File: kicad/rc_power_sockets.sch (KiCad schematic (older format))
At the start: 24 parts, among them IC1 ATTINY85, J1 PIR, J2 433MHZ, J3 433MHZ, P1 ICSP, P2 CONN_GND, Q1 NMOS, Q2 PMOS, SW1 SPST, U1 MCP1700T

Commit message: Schematic update
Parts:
- MOUNT1, MOUNT2, MOUNT3, MOUNT4: footprint (none) -> Wire_Pads:SolderWirePad_single_2-5mmDrill
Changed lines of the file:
@@
 F 0 "MOUNT3" V 1800 1100 50  0000 C CNN
 F 1 "CONN_01X01" V 1600 800 50  0001 C CNN
-F 2 "" H 1700 1100 50  0000 C CNN
+F 2 "Wire_Pads:SolderWirePad_single_2-5mmDrill" H 1700 1100 50  0001 C CNN
 F 3 "" H 1700 1100 50  0000 C CNN
 	1    1700 1100
@@
 F 0 "MOUNT4" V 2250 1100 50  0000 C CNN
 F 1 "CONN_01X01" V 2050 800 50  0001 C CNN
-F 2 "" H 2150 1100 50  0000 C CNN
+F 2 "Wire_Pads:SolderWirePad_single_2-5mmDrill" H 2150 1100 50  0001 C CNN
 F 3 "" H 2150 1100 50  0000 C CNN
 	1    2150 1100
@@
 F 0 "MOUNT1" V 950 1100 50  0000 C CNN
 F 1 "CONN_01X01" V 750 800 50  0001 C CNN
-F 2 "" H 850 1100 50  0000 C CNN
+F 2 "Wire_Pads:SolderWirePad_single_2-5mmDrill" H 850 1100 50  0001 C CNN
 F 3 "" H 850 1100 50  0000 C CNN
 	1    850  1100
@@
 F 0 "MOUNT2" V 1400 1100 50  0000 C CNN
 F 1 "CONN_01X01" V 1200 800 50  0001 C CNN
-F 2 "" H 1300 1100 50  0000 C CNN
+F 2 "Wire_Pads:SolderWirePad_single_2-5mmDrill" H 1300 1100 50  0001 C CNN
 F 3 "" H 1300 1100 50  0000 C CNN
 	1    1300 1100

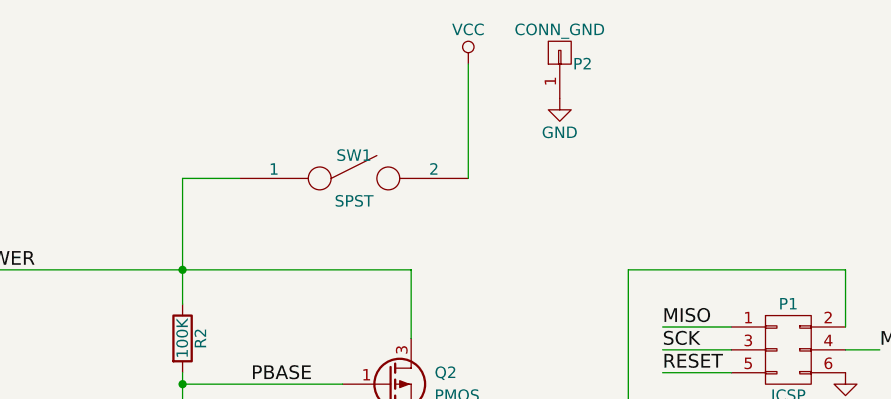
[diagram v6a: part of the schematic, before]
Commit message: Moved silkscreens
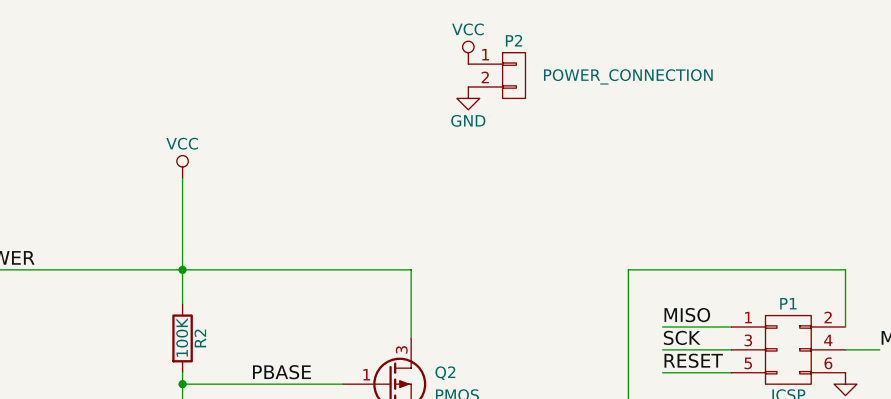
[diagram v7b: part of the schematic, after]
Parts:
- removed P2: CONN_GND, Pin_Headers:Pin_Header_Straight_1x01, symbol CONN_01X01
- removed SW1: SPST, Pin_Headers:Pin_Header_Straight_1x02, symbol SPST
- added P2: POWER_CONNECTION, Pin_Headers:Pin_Header_Straight_1x02, symbol CONN_01X02
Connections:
- net POWER is gone; now on net VCC: J1.3, Q2.3 (D), R2.1
- net GND: now also P2.2 (P2)
- net VCC: now also P2.1 (P1)
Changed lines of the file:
@@
 L VCC #PWR09
 U 1 1 56E80BFE
-P 6800 1050
-F 0 "#PWR09" H 6800 900 50  0001 C CNN
-F 1 "VCC" H 6800 1200 50  0000 C CNN
-F 2 "" H 6800 1050 50  0000 C CNN
-F 3 "" H 6800 1050 50  0000 C CNN
-	1    6800 1050
+P 5550 1550
+F 0 "#PWR09" H 5550 1400 50  0001 C CNN
+F 1 "VCC" H 5550 1700 50  0000 C CNN
+F 2 "" H 5550 1550 50  0000 C CNN
+F 3 "" H 5550 1550 50  0000 C CNN
+	1    5550 1550
 	1    0    0    -1
 $EndComp
@@
 F 3 "" H 7350 3900 50  0000 C CNN
 	1    7350 3900
-	1    0    0    -1
-$EndComp
-$Comp
-L SPST SW1
-U 1 1 56EAAC50
-P 6300 1550
-F 0 "SW1" H 6300 1650 50  0000 C CNN
-F 1 "SPST" H 6300 1450 50  0000 C CNN
-F 2 "Pin_Headers:Pin_Header_Straight_1x02" H 6300 1550 50  0001 C CNN
-F 3 "" H 6300 1550 50  0000 C CNN
-	1    6300 1550
 	1    0    0    -1
 $EndComp
@@
 NBASE
 $Comp
-L CONN_01X01 P2
-U 1 1 56EEF3F5
-P 7200 1000
-F 0 "P2" V 7150 900 50  0000 C CNN
-F 1 "CONN_GND" V 7300 1000 50  0000 C CNN
-F 2 "Pin_Headers:Pin_Header_Straight_1x01" H 7200 1000 50  0001 C CNN
-F 3 "" H 7200 1000 50  0000 C CNN
-	1    7200 1000
-	0    -1   -1   0
-$EndComp
-$Comp
 L GND #PWR010
 U 1 1 56EEF4F7
-P 7200 1200
-F 0 "#PWR010" H 7200 950 50  0001 C CNN
-F 1 "GND" H 7200 1050 50  0000 C CNN
-F 2 "" H 7200 1200 50  0000 C CNN
-F 3 "" H 7200 1200 50  0000 C CNN
-	1    7200 1200
+P 6800 1150
+F 0 "#PWR010" H 6800 900 50  0001 C CNN
+F 1 "GND" H 6800 1000 50  0000 C CNN
+F 2 "" H 6800 1150 50  0000 C CNN
+F 3 "" H 6800 1150 50  0000 C CNN
+	1    6800 1150
 	1    0    0    -1
 $EndComp
@@
 	4100 5550 4900 5550
 Wire Wire Line
-	6800 1050 6800 1550
-Wire Wire Line
 	4900 5450 4300 5450
 Wire Wire Line
@@
 Wire Wire Line
 	4150 3600 4150 5150
-Wire Wire Line
-	5550 1550 5800 1550
 Wire Wire Line
 	4650 3150 4150 3150
@@
 	1    0    0    -1
 $EndComp
+$Comp
+L VCC #PWR016
+U 1 1 56F0619B
+P 6800 1050
+F 0 "#PWR016" H 6800 900 50  0001 C CNN
+F 1 "VCC" H 6800 1200 50  0000 C CNN
+F 2 "" H 6800 1050 50  0000 C CNN
+F 3 "" H 6800 1050 50  0000 C CNN
+	1    6800 1050
+	1    0    0    -1
+$EndComp
+$Comp
+L CONN_01X02 P2
+U 1 1 56F0648D
+P 7000 1100
+F 0 "P2" H 7000 1250 50  0000 C CNN
+F 1 "POWER_CONNECTION" H 7500 1100 50  0000 C CNN
+F 2 "Pin_Headers:Pin_Header_Straight_1x02" H 7000 1100 50  0001 C CNN
+F 3 "" H 7000 1100 50  0000 C CNN
+	1    7000 1100
+	1    0    0    -1
+$EndComp

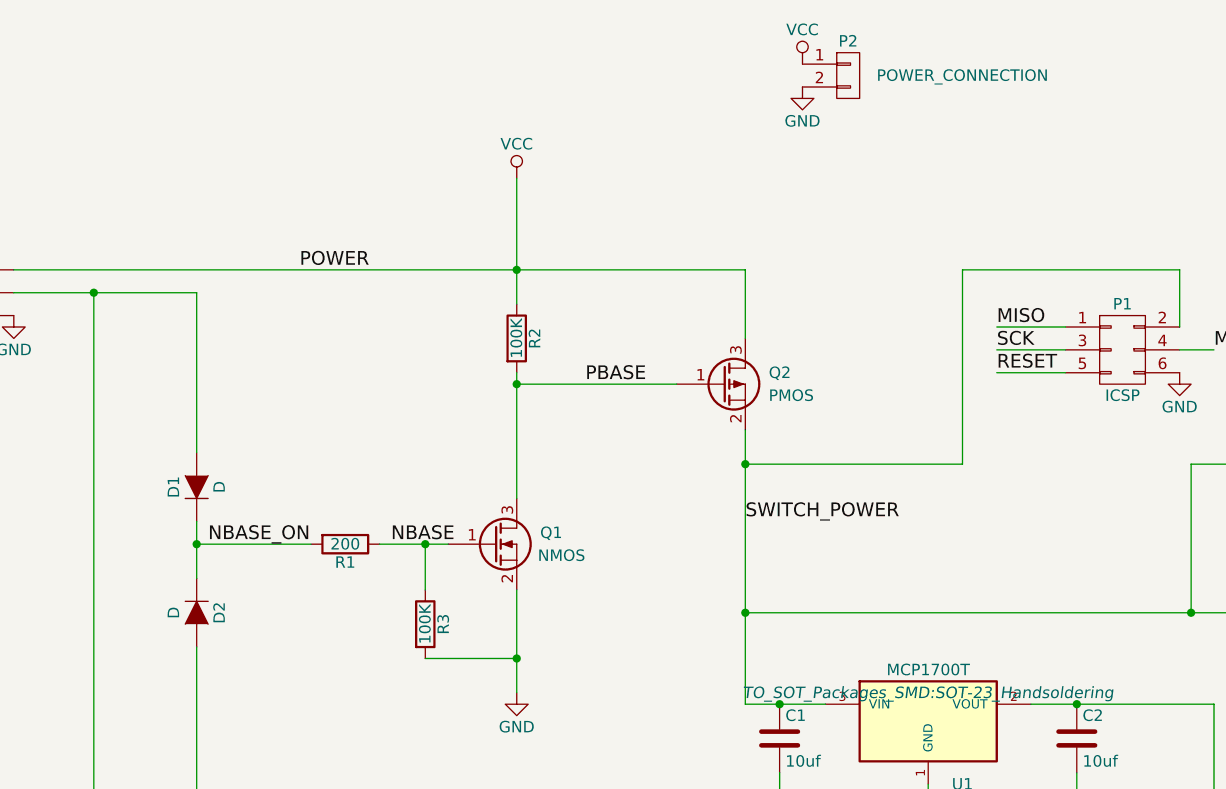
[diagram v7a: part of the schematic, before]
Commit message: M3 mounting holes
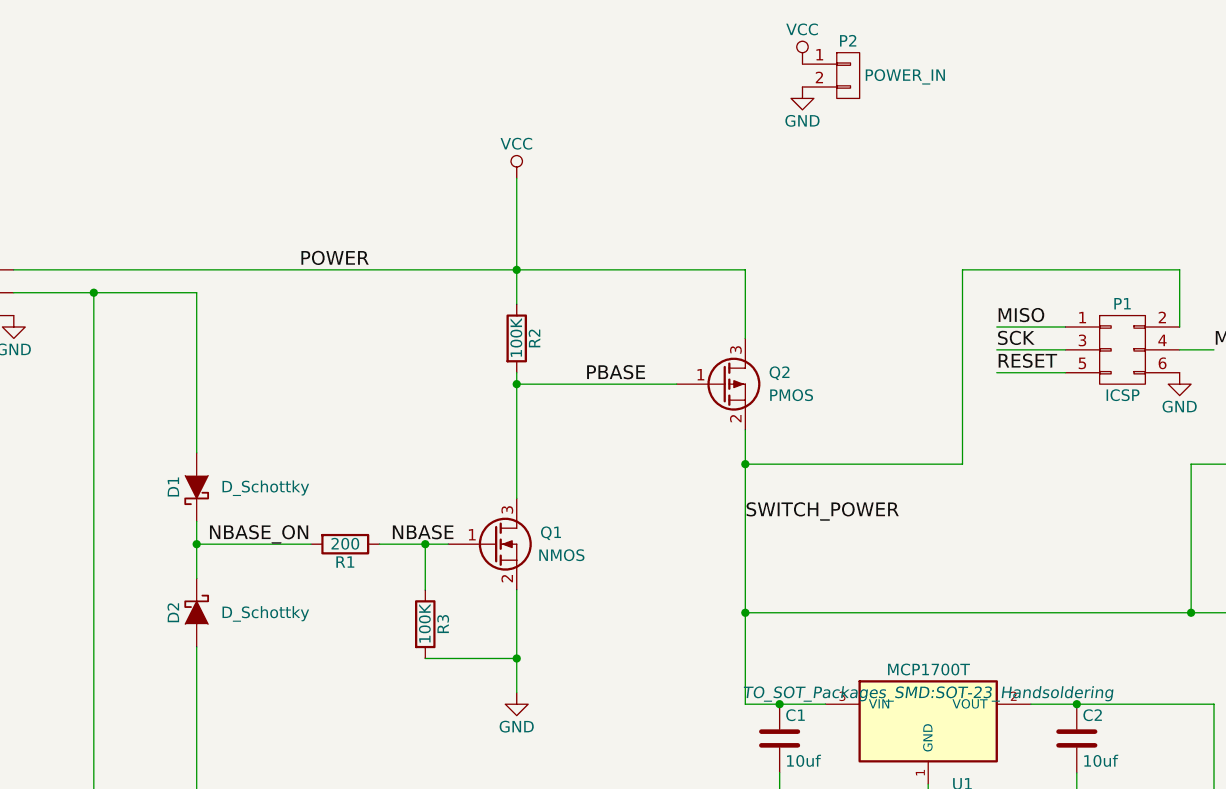
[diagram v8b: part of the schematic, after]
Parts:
- removed D1, D2: D, Diodes_SMD:SOD-123, symbol D
- added D1, D2: D_Schottky, Diodes_SMD:SOD-123, symbol D_Schottky
- MOUNT1, MOUNT2, MOUNT3, MOUNT4: footprint Wire_Pads:SolderWirePad_single_2-5mmDrill -> Mounting_Holes:MountingHole_3.2mm_M3_Pad
- P2: value POWER_CONNECTION -> POWER_IN
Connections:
- net MISO: now also D2.2 (A)
- net NBASE_ON: now also D1.1 (K), D2.1 (K)
- net SCK: now also D1.2 (A)
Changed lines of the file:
@@
 	1    0    0    -1
-$EndComp
-$Comp
-L D D1
-U 1 1 56D4EC51
-P 4150 2900
-F 0 "D1" H 4150 3000 50  0000 C CNN
-F 1 "D" H 4150 2800 50  0000 C CNN
-F 2 "Diodes_SMD:SOD-123" H 4150 2900 50  0001 C CNN
-F 3 "" H 4150 2900 50  0000 C CNN
-	1    4150 2900
-	0    -1   -1   0
-$EndComp
-$Comp
-L D D2
-U 1 1 56D4ECB1
-P 4150 3450
-F 0 "D2" H 4150 3550 50  0000 C CNN
-F 1 "D" H 4150 3350 50  0000 C CNN
-F 2 "Diodes_SMD:SOD-123" H 4150 3450 50  0001 C CNN
-F 3 "" H 4150 3450 50  0000 C CNN
-	1    4150 3450
-	0    1    1    0
 $EndComp
 Text Label 4300 5250 0    60   ~ 0
@@
 F 0 "MOUNT3" V 1800 1100 50  0000 C CNN
 F 1 "CONN_01X01" V 1600 800 50  0001 C CNN
-F 2 "Wire_Pads:SolderWirePad_single_2-5mmDrill" H 1700 1100 50  0001 C CNN
+F 2 "Mounting_Holes:MountingHole_3.2mm_M3_Pad" H 1700 1100 50  0001 C CNN
 F 3 "" H 1700 1100 50  0000 C CNN
 	1    1700 1100
@@
 F 0 "MOUNT4" V 2250 1100 50  0000 C CNN
 F 1 "CONN_01X01" V 2050 800 50  0001 C CNN
-F 2 "Wire_Pads:SolderWirePad_single_2-5mmDrill" H 2150 1100 50  0001 C CNN
+F 2 "Mounting_Holes:MountingHole_3.2mm_M3_Pad" H 2150 1100 50  0001 C CNN
 F 3 "" H 2150 1100 50  0000 C CNN
 	1    2150 1100
@@
 F 0 "MOUNT1" V 950 1100 50  0000 C CNN
 F 1 "CONN_01X01" V 750 800 50  0001 C CNN
-F 2 "Wire_Pads:SolderWirePad_single_2-5mmDrill" H 850 1100 50  0001 C CNN
+F 2 "Mounting_Holes:MountingHole_3.2mm_M3_Pad" H 850 1100 50  0001 C CNN
 F 3 "" H 850 1100 50  0000 C CNN
 	1    850  1100
@@
 F 0 "MOUNT2" V 1400 1100 50  0000 C CNN
 F 1 "CONN_01X01" V 1200 800 50  0001 C CNN
-F 2 "Wire_Pads:SolderWirePad_single_2-5mmDrill" H 1300 1100 50  0001 C CNN
+F 2 "Mounting_Holes:MountingHole_3.2mm_M3_Pad" H 1300 1100 50  0001 C CNN
 F 3 "" H 1300 1100 50  0000 C CNN
 	1    1300 1100
@@
 P 7000 1100
 F 0 "P2" H 7000 1250 50  0000 C CNN
-F 1 "POWER_CONNECTION" H 7500 1100 50  0000 C CNN
+F 1 "POWER_IN" H 7250 1100 50  0000 C CNN
 F 2 "Pin_Headers:Pin_Header_Straight_1x02" H 7000 1100 50  0001 C CNN
 F 3 "" H 7000 1100 50  0000 C CNN
@@
 	1    0    0    -1
 $EndComp
+$Comp
+L D_Schottky D1
+U 1 1 56F14591
+P 4150 2900
+F 0 "D1" H 4150 3000 50  0000 C CNN
+F 1 "D_Schottky" V 4150 2600 50  0000 C CNN
+F 2 "Diodes_SMD:SOD-123" H 4150 2900 50  0001 C CNN
+F 3 "" H 4150 2900 50  0000 C CNN
+	1    4150 2900
+	0    -1   -1   0
+$EndComp
+$Comp
+L D_Schottky D2
+U 1 1 56F1471B
+P 4150 3450
+F 0 "D2" H 4150 3350 50  0000 C CNN
+F 1 "D_Schottky" V 4150 3750 50  0000 C CNN
+F 2 "Diodes_SMD:SOD-123" H 4150 3450 50  0001 C CNN
+F 3 "" H 4150 3450 50  0000 C CNN
+	1    4150 3450
+	0    1    1    0
+$EndComp
 $EndSCHEMATC
